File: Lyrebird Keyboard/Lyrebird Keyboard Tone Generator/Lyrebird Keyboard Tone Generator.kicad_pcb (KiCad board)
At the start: 2 copper layers, 76.8 x 75.2 mm, 111 parts, among them IC1 LM358DT, IC10 LM358DT, IC11 LM358DT, IC12 LM358DT, IC13 HEF4069UBT,653, IC14 HEF4069UBT,653, IC2 LM358DT, IC3 LM358DT, IC4 LM358DT, IC5 LM358DT, IC6 LM358DT, IC7 LM358DT, IC8 LM358DT, IC9 LM358DT, J1 Edge Connector, J10 C# 4434 Hz, J11 G# 6642 Hz, J12 D 4697 Hz, J13 F# 5923 Hz, J2 A 3520 Hz, J3 D# 4976 Hz, J4 A# 3726 Hz, J5 E 5274 Hz, J6 B 3949 Hz, J7 F 5590 Hz, J8 C 4188 Hz, J9 G 6275 Hz

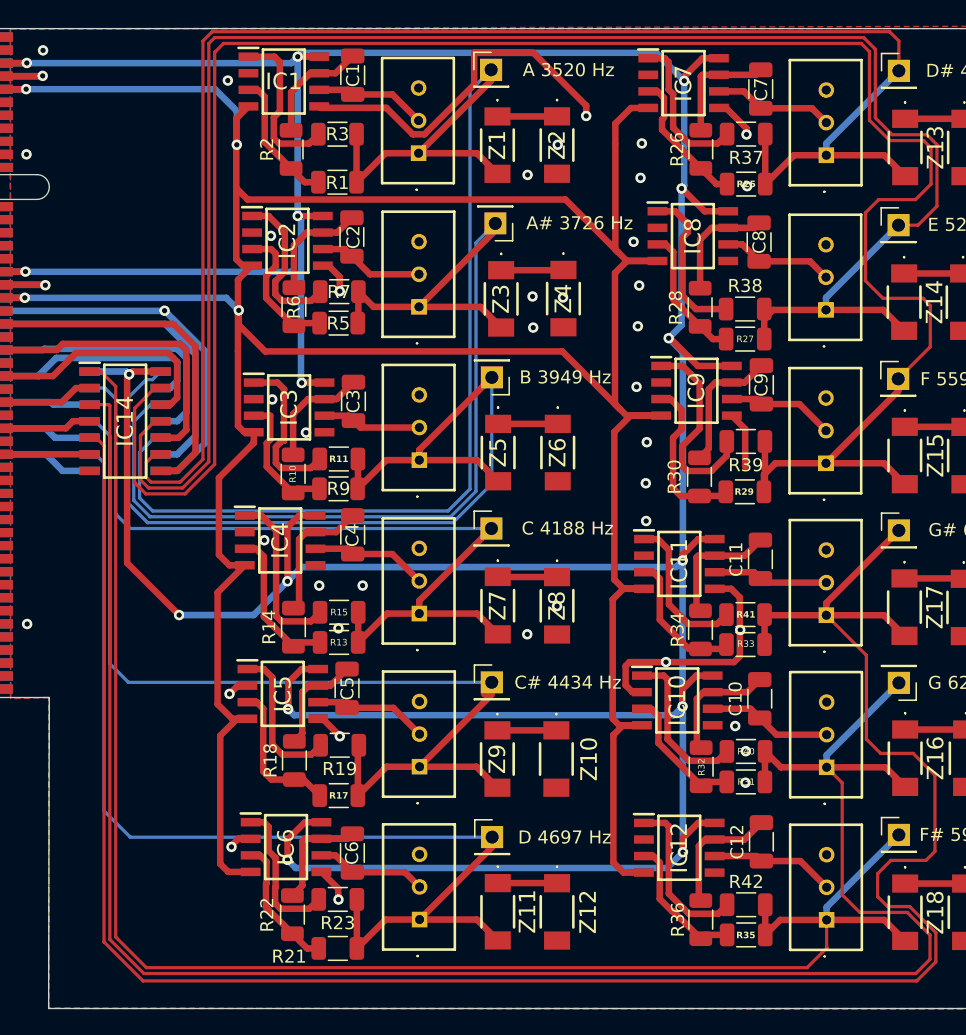
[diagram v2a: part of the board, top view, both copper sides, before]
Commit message: Move PSU and Amp off of mainboard
Moved Power Supply to its own board, single layer.  Moved Class D amp onto a daughter board, modifiying to also have a 1/4" balanced output as well as amplified output
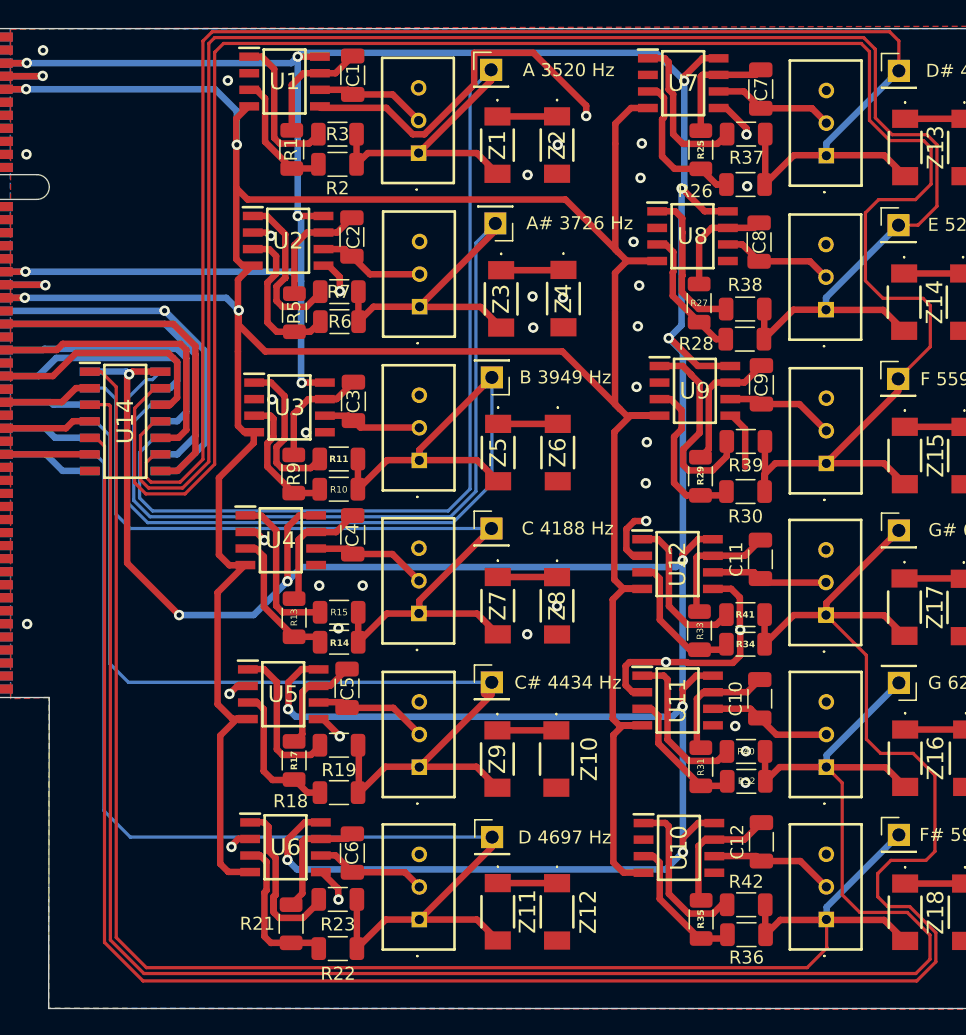
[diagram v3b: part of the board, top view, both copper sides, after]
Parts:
- removed IC1, IC10, IC11, IC12, IC2, IC3, IC4, IC5, IC6, IC7, IC8, IC9: LM358DT, SamacSys_Parts:SOIC127P600X175-8N
- removed IC13, IC14: HEF4069UBT,653, SamacSys_Parts:SOIC127P600X175-14N
- added U1: LM358, SamacSys_Parts:SOIC127P600X175-8N, F.Cu at (124.3, 57.7)
- added U10: LM358, SamacSys_Parts:SOIC127P600X175-8N, F.Cu at (154.5, 116.4)
- added U11: LM358, SamacSys_Parts:SOIC127P600X175-8N, F.Cu at (154.4, 105.1)
- added U12: LM358, SamacSys_Parts:SOIC127P600X175-8N, F.Cu at (154.4, 94.7)
- added U13: 4069, SamacSys_Parts:SOIC127P600X175-14N, B.Cu at (112.0, 83.7)
- added U14: 4069, SamacSys_Parts:SOIC127P600X175-14N, F.Cu at (112.1, 83.7)
- added U2: LM358, SamacSys_Parts:SOIC127P600X175-8N, F.Cu at (124.6, 69.9)
- added U3: LM358, SamacSys_Parts:SOIC127P600X175-8N, F.Cu at (124.7, 82.7)
- added U4: LM358, SamacSys_Parts:SOIC127P600X175-8N, F.Cu at (124.0, 92.8)
- added U5: LM358, SamacSys_Parts:SOIC127P600X175-8N, F.Cu at (124.2, 104.6)
- added U6: LM358, SamacSys_Parts:SOIC127P600X175-8N, F.Cu at (124.4, 116.4)
- added U7: LM358, SamacSys_Parts:SOIC127P600X175-8N, F.Cu at (154.9, 57.8)
- added U8: LM358, SamacSys_Parts:SOIC127P600X175-8N, F.Cu at (155.6, 69.5)
- added U9: LM358, SamacSys_Parts:SOIC127P600X175-8N, F.Cu at (155.8, 81.4)
- moved R27 4.48 mm to (156.1, 74.7), turned to -90 degrees
- moved R25 4.37 mm to (156.2, 62.9), turned to -90 degrees
- moved R26 4.36 mm to (159.6, 65.6), turned to 0 degrees
- moved R17 4.36 mm to (125.0, 109.7), turned to -90 degrees
- moved R22 4.35 mm to (128.4, 124.2), turned to 0 degrees
- moved R1 4.32 mm to (124.8, 62.9), turned to -90 degrees
- moved R18 4.22 mm to (128.5, 112.2), turned to 0 degrees
- moved R28 4.21 mm to (159.6, 77.4), turned to 0 degrees
- moved R21 4.05 mm to (124.8, 122.3), turned to -90 degrees
- moved R13 3.94 mm to (125.0, 98.8), turned to -90 degrees
- moved R2 3.73 mm to (128.3, 64.0), turned to 0 degrees
- moved R30 3.71 mm to (159.6, 89.1), turned to 0 degrees
- moved R10 3.69 mm to (128.4, 88.9), turned to 0 degrees
- moved R36 3.69 mm to (159.7, 123.1), turned to 0 degrees
- moved R14 3.69 mm to (128.5, 100.7), turned to 0 degrees
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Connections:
- C1 pad 2: TRI WAVE OUT (A) -> Net-(C1-Pad2)
- C10 pad 2: TRI WAVE OUT (G) -> Net-(C10-Pad2)
- C11 pad 2: TRI WAVE OUT (G#) -> Net-(C11-Pad2)
- C12 pad 2: TRI WAVE OUT (F#) -> Net-(C12-Pad2)
- C2 pad 2: TRI WAVE OUT (A#) -> Net-(C2-Pad2)
- C3 pad 2: TRI WAVE OUT (B) -> Net-(C3-Pad2)
- C4 pad 2: TRI WAVE OUT (C) -> Net-(C4-Pad2)
- C5 pad 2: TRI WAVE OUT (C#) -> Net-(C5-Pad2)
- C6 pad 2: TRI WAVE OUT (D) -> Net-(C6-Pad2)
- C7 pad 2: TRI WAVE OUT (D#) -> Net-(C7-Pad2)
- C8 pad 2: TRI WAVE OUT (E) -> Net-(C8-Pad2)
- C9 pad 2: TRI WAVE OUT (F) -> Net-(C9-Pad2)
- R1 pad 1: Net-(IC1-IN1+) -> Net-(C1-Pad2)
- R1 pad 2: A (3520 Hz) -> Net-(U1A-+)
- R10 pad 1: TRI WAVE OUT (B) -> Net-(U3A-+)
- R10 pad 2: Net-(IC3-IN1+) -> B (3949 Hz)
- R11 pad 1: B (3949 Hz) -> Net-(R11-Pad1)
- R11 pad 2: Net-(IC3-OUT1) -> B (3949 Hz)
- R13 pad 1: Net-(IC4-IN1+) -> Net-(C4-Pad2)
- R13 pad 2: C (4188 Hz) -> Net-(U4A-+)
- R14 pad 1: TRI WAVE OUT (C) -> Net-(U4A-+)
- R14 pad 2: Net-(IC4-IN1+) -> C (4188 Hz)
- R15 pad 1: C (4188 Hz) -> Net-(R15-Pad1)
- R15 pad 2: Net-(IC4-OUT1) -> C (4188 Hz)
- R17 pad 1: Net-(IC5-IN1+) -> Net-(C5-Pad2)
- R17 pad 2: C# (4434 Hz) -> Net-(U5A-+)
- R18 pad 1: TRI WAVE OUT (C#) -> Net-(U5A-+)
- R18 pad 2: Net-(IC5-IN1+) -> C# (4434 Hz)
- R19 pad 1: C# (4434 Hz) -> Net-(R19-Pad1)
- R19 pad 2: Net-(IC5-OUT1) -> C# (4434 Hz)
- R2 pad 1: TRI WAVE OUT (A) -> Net-(U1A-+)
- R2 pad 2: Net-(IC1-IN1+) -> A (3520 Hz)
- R21 pad 1: Net-(IC6-IN1+) -> Net-(C6-Pad2)
- R21 pad 2: D (4697 Hz) -> Net-(U6A-+)
- R22 pad 1: TRI WAVE OUT (D) -> Net-(U6A-+)
- R22 pad 2: Net-(IC6-IN1+) -> D (4697 Hz)
- R23 pad 1: D (4697 Hz) -> Net-(R23-Pad1)
- R23 pad 2: Net-(IC6-OUT1) -> D (4697 Hz)
- R25 pad 1: Net-(IC7-IN1+) -> Net-(C7-Pad2)
- R25 pad 2: D# (4976 Hz) -> Net-(U7A-+)
- R26 pad 1: TRI WAVE OUT (D#) -> Net-(U7A-+)
- R26 pad 2: Net-(IC7-IN1+) -> D# (4976 Hz)
- R27 pad 1: Net-(IC8-IN1+) -> Net-(C8-Pad2)
- R27 pad 2: E (5274 Hz) -> Net-(U8A-+)
- R28 pad 1: TRI WAVE OUT (E) -> Net-(U8A-+)
- R28 pad 2: Net-(IC8-IN1+) -> E (5274 Hz)
- R29 pad 1: Net-(IC9-IN1+) -> Net-(C9-Pad2)
- R29 pad 2: F (5590 Hz) -> Net-(U9A-+)
- R3 pad 1: A (3520 Hz) -> Net-(R3-Pad1)
- R3 pad 2: Net-(IC1-OUT1) -> A (3520 Hz)
- R30 pad 1: TRI WAVE OUT (F) -> Net-(U9A-+)
- R30 pad 2: Net-(IC9-IN1+) -> F (5590 Hz)
- R31 pad 1: Net-(IC10-IN1+) -> Net-(C10-Pad2)
- R31 pad 2: G (6275 Hz) -> Net-(U11A-+)
- R32 pad 1: TRI WAVE OUT (G) -> Net-(U11A-+)
- R32 pad 2: Net-(IC10-IN1+) -> G (6275 Hz)
- R33 pad 1: Net-(IC11-IN1+) -> Net-(C11-Pad2)
- R33 pad 2: G# (6642 Hz) -> Net-(U12A-+)
- R34 pad 1: TRI WAVE OUT (G#) -> Net-(U12A-+)
- R34 pad 2: Net-(IC11-IN1+) -> G# (6642 Hz)
- R35 pad 1: Net-(IC12-IN1+) -> Net-(C12-Pad2)
- R35 pad 2: F# (5923 Hz) -> Net-(U10A-+)
- R36 pad 1: TRI WAVE OUT (F#) -> Net-(U10A-+)
- R36 pad 2: Net-(IC12-IN1+) -> F# (5923 Hz)
- R37 pad 1: D# (4976 Hz) -> Net-(R37-Pad1)
- R37 pad 2: Net-(IC7-OUT1) -> D# (4976 Hz)
- R38 pad 1: E (5274 Hz) -> Net-(R38-Pad1)
- R38 pad 2: Net-(IC8-OUT1) -> E (5274 Hz)
- R39 pad 1: F (5590 Hz) -> Net-(R39-Pad1)
- R39 pad 2: Net-(IC9-OUT1) -> F (5590 Hz)
- R40 pad 1: G (6275 Hz) -> Net-(R40-Pad1)
- R40 pad 2: Net-(IC10-OUT1) -> G (6275 Hz)
- R41 pad 1: G# (6642 Hz) -> Net-(R41-Pad1)
- R41 pad 2: Net-(IC11-OUT1) -> G# (6642 Hz)
- R42 pad 1: F# (5923 Hz) -> Net-(R42-Pad1)
- R42 pad 2: Net-(IC12-OUT1) -> F# (5923 Hz)
- R5 pad 1: Net-(IC2-IN1+) -> Net-(C2-Pad2)
- R5 pad 2: A# (3726 Hz) -> Net-(U2A-+)
- R6 pad 1: TRI WAVE OUT (A#) -> Net-(U2A-+)
- R6 pad 2: Net-(IC2-IN1+) -> A# (3726 Hz)
- R7 pad 1: A# (3726 Hz) -> Net-(R7-Pad1)
- R7 pad 2: Net-(IC2-OUT1) -> A# (3726 Hz)
- R9 pad 1: Net-(IC3-IN1+) -> Net-(C3-Pad2)
- R9 pad 2: B (3949 Hz) -> Net-(U3A-+)
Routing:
- net Net-(IC9-OUT1): track 15.6 -> 0.00 mm
- net Net-(R39-Pad1): track 0.00 -> 15.4 mm
- net Net-(R23-Pad1): track 0.00 -> 13.8 mm
- net Net-(IC4-OUT1): track 13.3 -> 0.00 mm
- net Net-(IC9-IN1+): track 12.6 -> 0.00 mm
- net Net-(IC12-OUT1): track 12.6 -> 0.00 mm
- net Net-(R7-Pad1): track 0.00 -> 12.6 mm
- net Net-(R42-Pad1): track 0.00 -> 12.6 mm
- net Net-(IC1-OUT1): track 12.5 -> 0.00 mm
- net Net-(IC3-OUT1): track 12.4 -> 0.00 mm
- net Net-(U9A-+): track 0.00 -> 12.3 mm
- net Net-(R40-Pad1): track 0.00 -> 12.2 mm
- net Net-(R15-Pad1): track 0.00 -> 12.2 mm
- net Net-(IC10-OUT1): track 12.2 -> 0.00 mm
- net Net-(IC8-OUT1): track 12.2 -> 0.00 mm
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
